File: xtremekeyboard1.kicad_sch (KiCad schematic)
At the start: 58 parts, among them SW1 1u MX, SW10 1u MX, SW11 1u MX, SW12 1u MX, SW13 1u MX, SW14 1u MX, SW15 1u MX, SW16 1u MX, SW17 1u MX, SW18 1u MX, SW19 1u MX, SW2 1u MX, SW20 1u MX, SW21 1u MX, SW22 1u MX, SW23 1u MX, SW24 1u MX, SW25 1u MX, SW26 1u MX, SW27 1u MX, SW3 1u MX, SW4 1u MX, SW5 1u MX, SW6 1u MX, SW7 1u MX, SW8 1u MX, SW9 1u MX, U1 rp2040-zero

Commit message: pushing slight changes
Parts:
- JP1, JP2: footprint (none) -> Jumper:SolderJumper-2_P1.3mm_Open_TrianglePad1.0x1.5mm
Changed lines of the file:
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@@
       (effects (font (size 1.27 1.27)))
     )
-    (property "Footprint" "" (at 128.905 82.55 0)
+    (property "Footprint" "Jumper:SolderJumper-2_P1.3mm_Open_TrianglePad1.0x1.5mm" (at 128.905 82.55 0)
       (effects (font (size 1.27 1.27)) hide)
     )
@@
       (effects (font (size 1.27 1.27)))
     )
-    (property "Footprint" "" (at 140.335 82.55 0)
-      (effects (font (size 1.27 1.27)) hide)
-    )
+    (property "Footprint" "Jumper:SolderJumper-2_P1.3mm_Open_TrianglePad1.0x1.5mm" (at 140.335 82.55 0)
+      (effects (font (size 1.27 1.27)) hide)
+    )

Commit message: version 1, no display
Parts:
- added J2: Conn_01x05_Pin, keyboard:5_Solder_Pad, symbol Connector:Conn_01x05_Pin
- added J3: Conn_01x05_Socket, keyboard:5_Solder_Pad, symbol Connector:Conn_01x05_Socket
- added JP10, JP12, JP14, JP16, JP18, JP4, JP6, JP8: LJumper, Jumper:SolderJumper-2_P1.3mm_Open_TrianglePad1.0x1.5mm, symbol Jumper:SolderJumper_2_Bridged
- added JP11, JP13, JP15, JP17, JP3, JP5, JP7, JP9: RJumper, Jumper:SolderJumper-2_P1.3mm_Open_TrianglePad1.0x1.5mm, symbol Jumper:SolderJumper_2_Open
- added U2: PS4 Joystick, ps4_joystick:PS4_joystick, symbol keyboard:PS4_Joystick
- renumbered SW15 to SW14, SW17 to SW15, SW19 to SW16, SW21 to SW17, SW23 to SW18, SW14 to SW19, SW16 to SW20, SW18 to SW21, SW20 to SW22, SW22 to SW23
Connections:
- net +5V: now also JP1.2 (B); no longer JP1.1 (A)
- net COL0: now also JP5.1 (A), JP6.1 (A); no longer U1.4 (3)
- net COL1: now also JP10.1 (A), JP9.1 (A); no longer U1.5 (4)
- net COL2: now also JP13.1 (A), JP14.1 (A); no longer U1.6 (5)
- net COL3: now also JP17.1 (A), JP18.1 (A); no longer U1.7 (6)
- net GND: now also J3.5 (Pin_5)
- net ROW0: now also U1.11 (10); no longer U1.10 (9)
- net ROW1: now also U1.10 (9); no longer U1.11 (10)
- net at U1.1 (0): now also JP1.1 (A); no longer JP1.2 (B)
- net JOYSW: now reaches U1.16 (15)
- net JOYSW: now also J3.4 (Pin_4)
- net SDAa: now reaches U1.17 (26)
- net SDAa: now also JP16.2 (B), JP17.2 (B)
- net SCLa: now reaches U1.18 (27)
- net SCLa: now also JP12.2 (B), JP13.2 (B)
- net JXa: now reaches U1.19 (28)
- net JXa: now also JP8.2 (B), JP9.2 (B)
- net JYa: now reaches U1.20 (29)
- net JYa: now also JP4.2 (B), JP5.2 (B)
- net +3.3V: now reaches U1.21 (3V3)
- net +3.3V: now also U1.3 (2), J3.1 (Pin_1)
- new net +3.3V_JOY: J2.1 (Pin_1), U2.3 (VCC), U2.6 (VCC)
- new net GND_JOY: J2.5 (Pin_5), U2.2 (SW2), U2.5 (GND), U2.8 (GND)
- new net JOYSWb: J2.4 (Pin_4), U2.1 (SW1)
- new net JOYX: J3.2 (Pin_2), JP7.1 (A), JP8.1 (A)
- new net JOYXb: J2.2 (Pin_2), U2.7 (VRX)
- new net JOYY: J3.3 (Pin_3), JP3.1 (A), JP4.1 (A)
- new net JOYYb: J2.3 (Pin_3), U2.4 (VRY)
- new net JXb: JP10.2 (B), JP7.2 (B), U1.5 (4)
- new net JYb: JP3.2 (B), JP6.2 (B), U1.4 (3)
- new net SCL: JP11.1 (A), JP12.1 (A)
- new net SCLb: JP11.2 (B), JP14.2 (B), U1.6 (5)
- new net SDA: JP15.1 (A), JP16.1 (A)
- new net SDAb: JP15.2 (B), JP18.2 (B), U1.7 (6)
- no-connect marks 2 -> 0
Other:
- note added: "Analog Stick"
- note added: "Keyswitch Matrix"
- note added: "MCU"
- note added: "Signal Jumpers"
- note added: "TRS Jack"
- moved on the sheet: D1, D10, D11, D12, D13, D14, D15, D16, D17, D18, D19, D2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

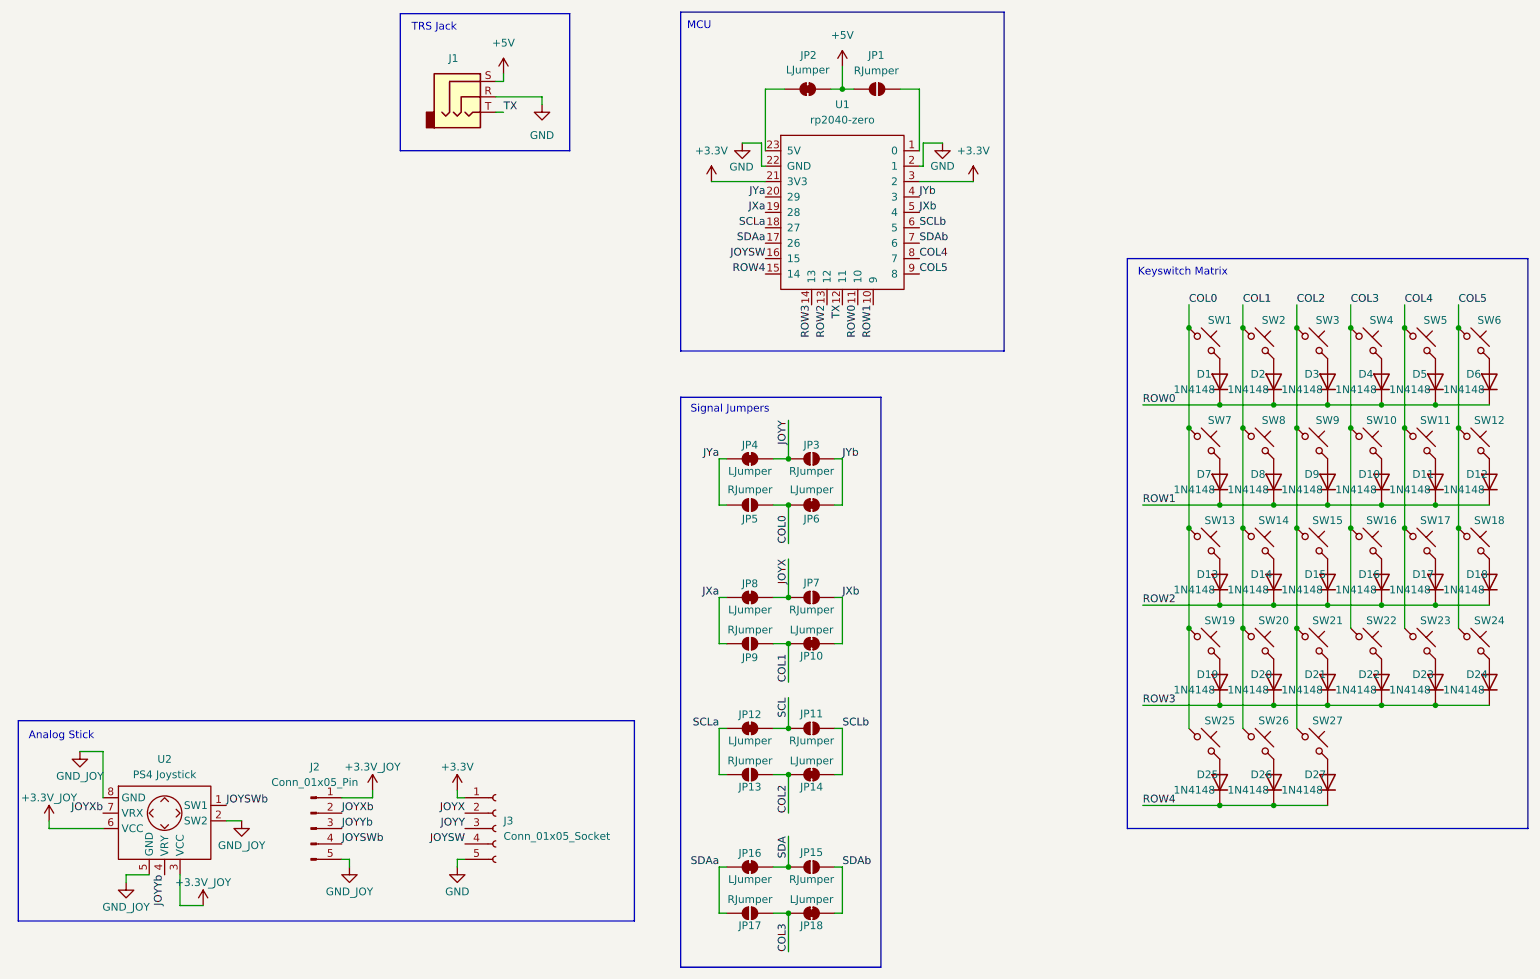
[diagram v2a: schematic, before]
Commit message: finished pcb routing
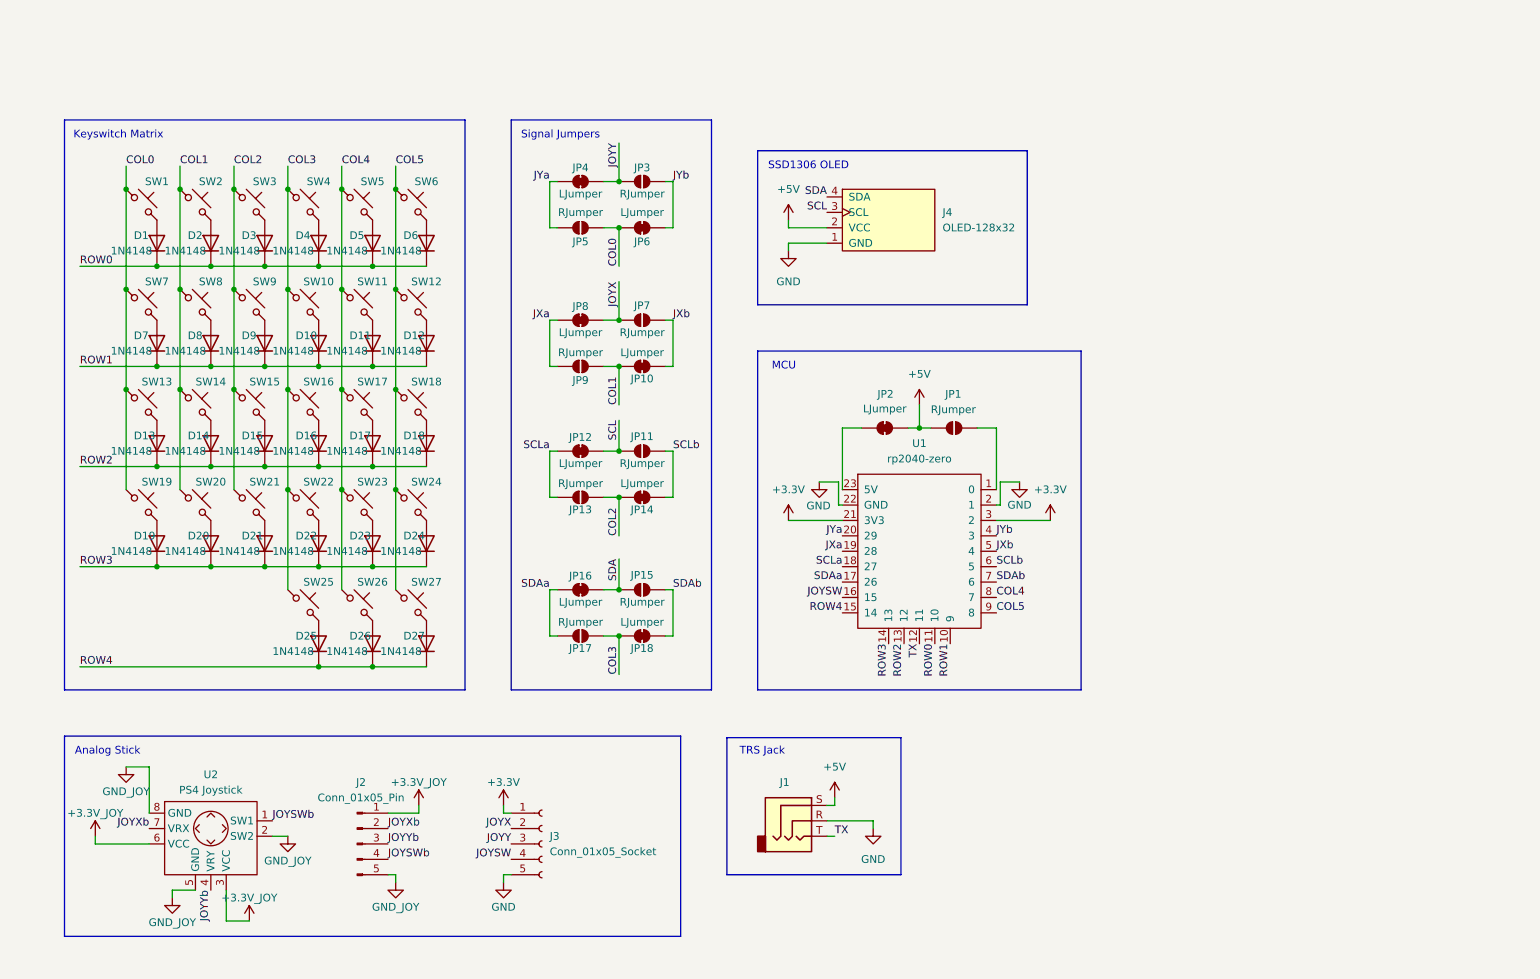
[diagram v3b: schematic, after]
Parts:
- added J4: OLED-128x32, display:OLED-128x32-cutout, symbol keyboard_display:OLED-128x32
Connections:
- net +5V: now also J4.2 (VCC)
- net COL0: no longer SW25.1
- net COL1: no longer SW26.1
- net COL2: no longer SW27.1
- net COL3: now also SW25.1
- net COL4: now also SW26.1
- net COL5: now also SW27.1
- net GND: now also J4.1 (GND)
- net SCL: now also J4.3 (SCL)
- net SDA: now also J4.4 (SDA)
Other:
- note added: "SSD1306 OLED"
- moved on the sheet: D1, D10, D11, D12, D13, D14, D15, D16, D17, D18, D19, D2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

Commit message: finished good pcb, need to make oled reversible, maybe put jumpers on respective side
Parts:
- added D28: 1N4148, Diode_THT:D_DO-35_SOD27_P7.62mm_Horizontal, symbol Diode:1N4148
- SW1, SW10, SW11, SW12, SW13, SW14, SW15, SW16, SW17, SW18, SW19, SW2, SW20, SW21, SW22, SW23, SW24, SW25, SW26, SW27, SW3, SW4, SW5, SW6, SW7, SW8, SW9: footprint PCM_Switch_Keyboard_Cherry_MX:SW_Cherry_MX_PCB_1.00u -> PCM_Switch_Keyboard_Cherry_MX:MX_PCB_Reversible; symbol keyboard:MX 1u PCB -> keyboard:MX_1u_PCB_Reversible
- U1: footprint keyboard_mcu:rp2040-zero-tht -> mcu:rp2040-zero-tht
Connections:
- net COL2: now also D28.2 (A)
- net ROW4: now also D28.1 (K)

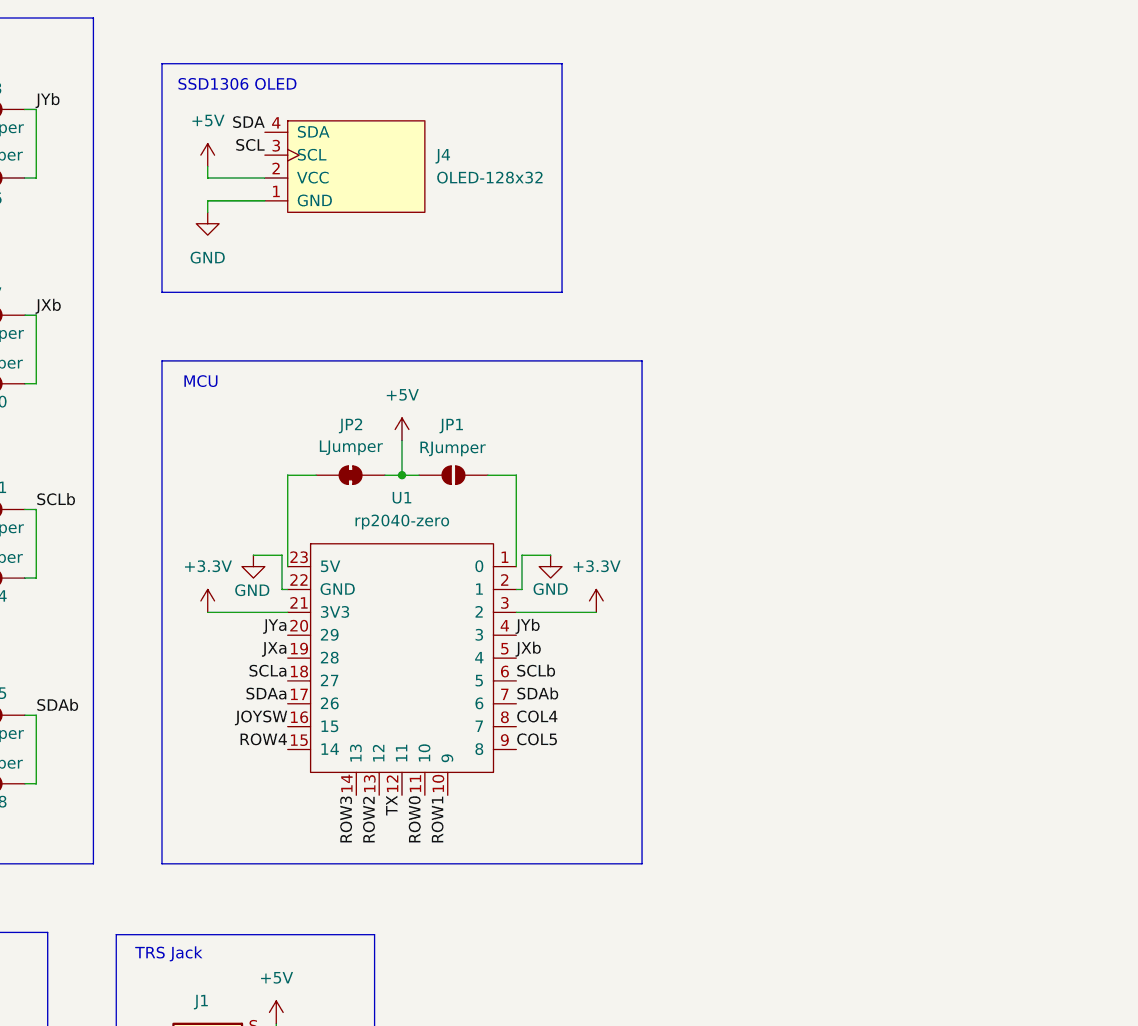
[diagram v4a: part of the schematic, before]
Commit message: added pullup resistors, fixed solder jumpers
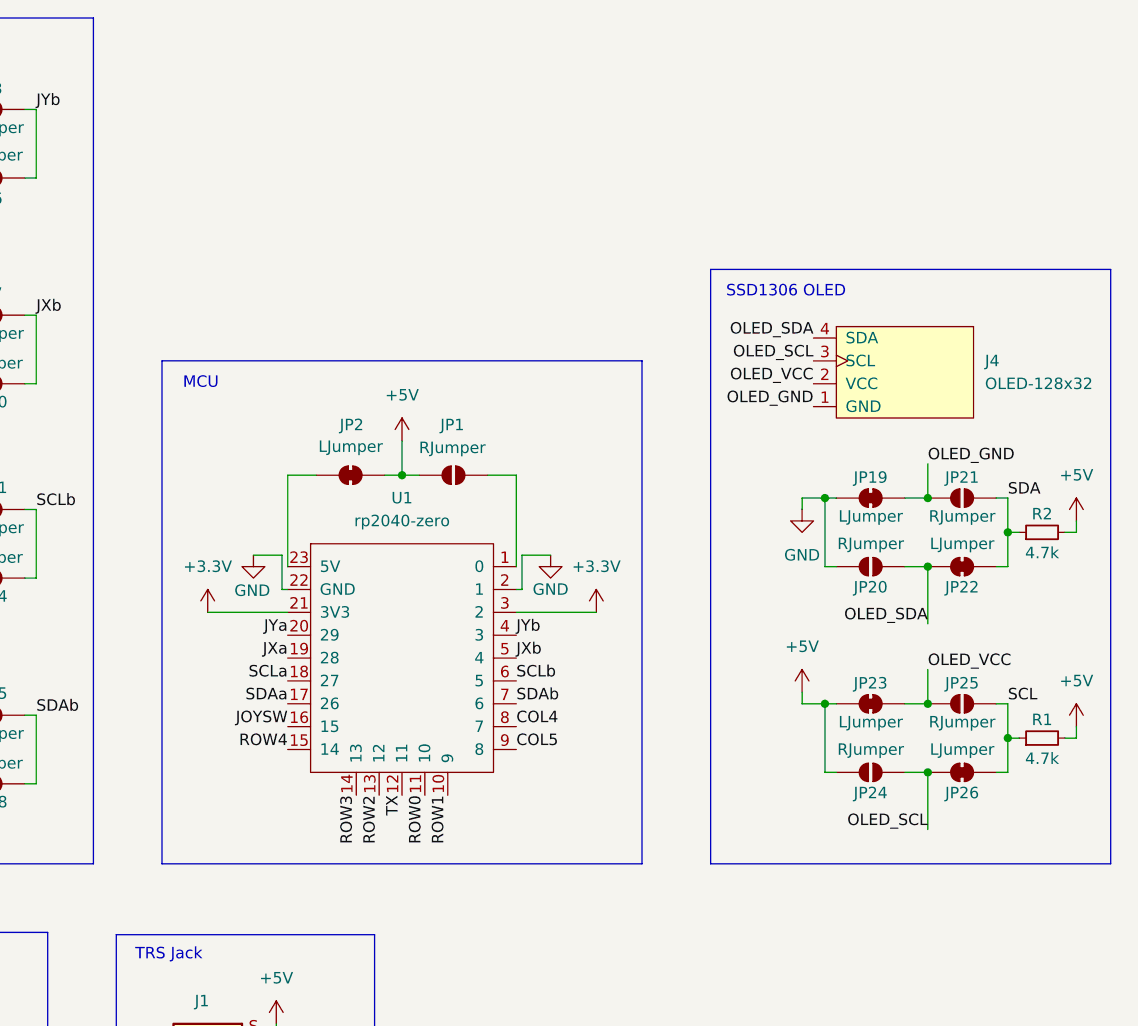
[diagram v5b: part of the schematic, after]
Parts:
- added JP19, JP22, JP23, JP26: LJumper, Jumper:SolderJumper-2_P1.3mm_Open_TrianglePad1.0x1.5mm, symbol Jumper:SolderJumper_2_Bridged
- added JP20, JP21, JP24, JP25: RJumper, Jumper:SolderJumper-2_P1.3mm_Open_TrianglePad1.0x1.5mm, symbol Jumper:SolderJumper_2_Open
- added R1, R2: 4.7k, Resistor_THT:R_Axial_DIN0204_L3.6mm_D1.6mm_P5.08mm_Horizontal, symbol Device:R_Small
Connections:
- net +5V: now also JP23.2 (B), JP24.2 (B), R1.2, R2.2; no longer J4.2 (VCC)
- net GND: now also JP19.2 (B), JP20.2 (B); no longer J4.1 (GND)
- net SCL: now also JP25.2 (B), JP26.2 (B), R1.1; no longer J4.3 (SCL)
- net SDA: now also JP21.2 (B), JP22.2 (B), R2.1; no longer J4.4 (SDA)
- new net OLED_GND: J4.1 (GND), JP19.1 (A), JP21.1 (A)
- new net OLED_SCL: J4.3 (SCL), JP24.1 (A), JP26.1 (A)
- new net OLED_SDA: J4.4 (SDA), JP20.1 (A), JP22.1 (A)
- new net OLED_VCC: J4.2 (VCC), JP23.1 (A), JP25.1 (A)
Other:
- moved on the sheet: J4
